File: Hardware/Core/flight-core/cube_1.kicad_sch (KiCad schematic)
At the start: 3 parts, among them J5 Cube Orange Plus Female Header

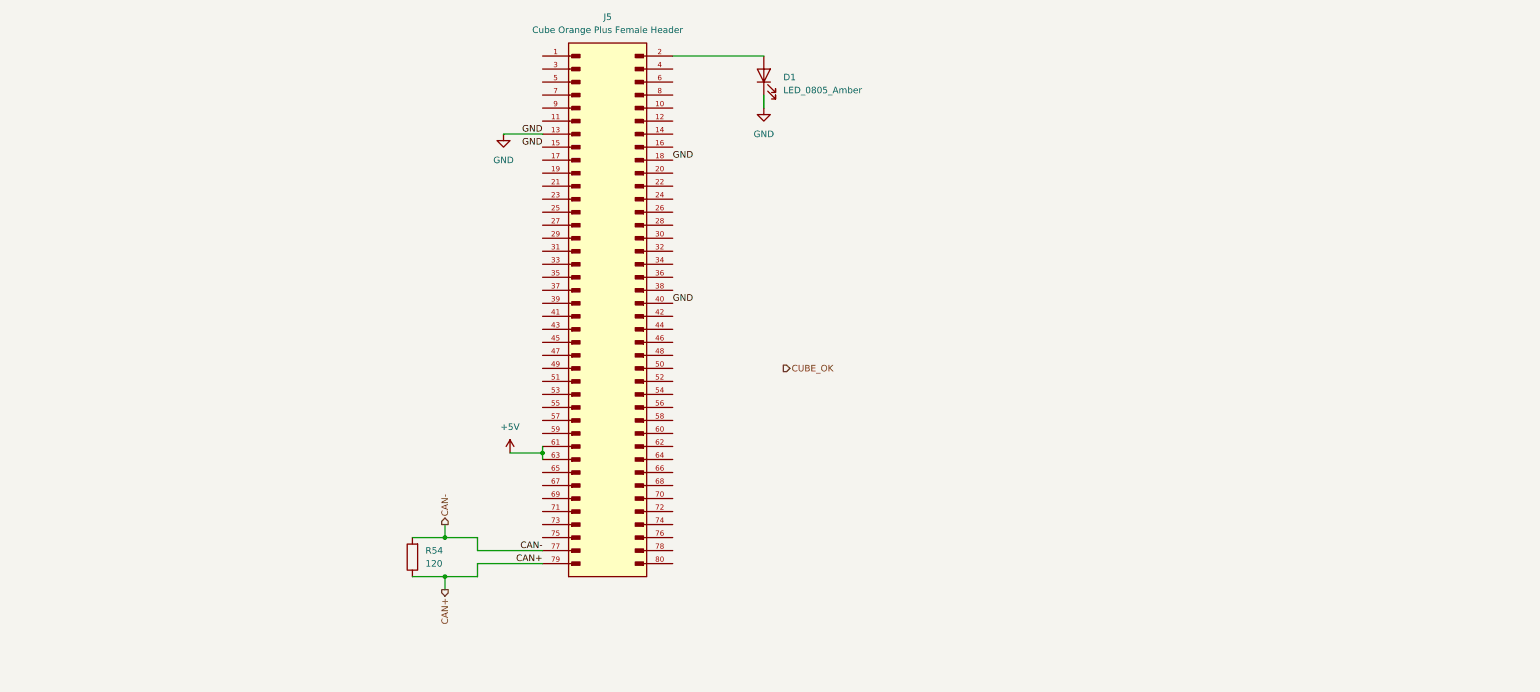
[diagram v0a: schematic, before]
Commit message: added all cube pins and corrected cube shdn node
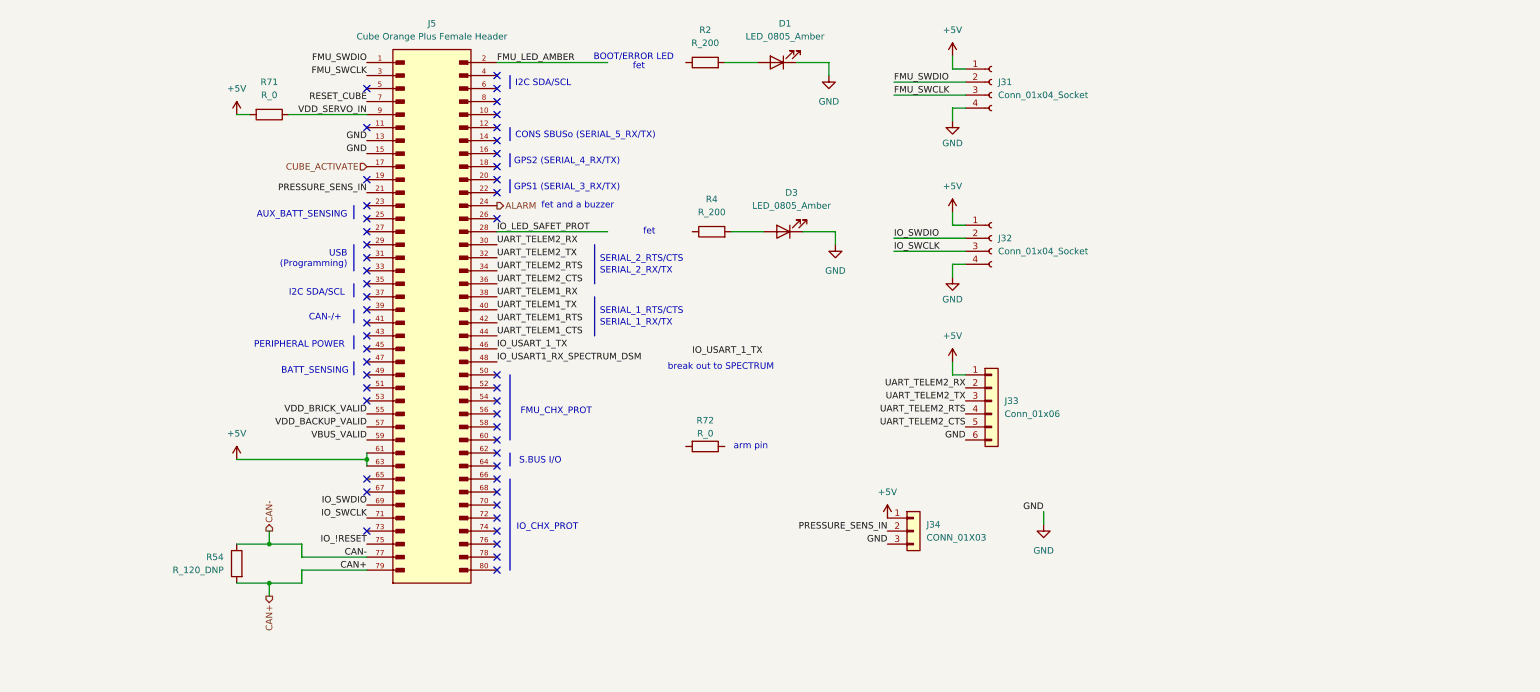
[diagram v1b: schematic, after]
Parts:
- removed R54: 120, OEM:R_0603, symbol OEM:120R
- added D3: LED_0805_Amber, footprints:LED_0805_OEM, symbol formula:LED_0805_Amber
- added J31, J32: Conn_01x04_Socket, Connector_PinSocket_2.54mm:PinSocket_1x04_P2.54mm_Vertical, symbol Connector:Conn_01x04_Socket
- added J33: Conn_01x06, symbol Connector_Generic:Conn_01x06
- added J34: CONN_01X03, Pin_Headers:Pin_Header_Straight_1x03_Pitch2.54mm, symbol formula:CONN_01X03
- added R2, R4: R_200, footprints:R_0603_1608Metric, symbol formula:R_200
- added R54: R_120_DNP, footprints:R_0603_1608Metric, symbol formula:R_120_DNP
- added R71, R72: R_0, footprints:R_0603_1608Metric, symbol formula:R_0
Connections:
- net +5V: now also J31.1 (Pin_1), J32.1 (Pin_1), J33.1 (Pin_1), J34.1 (P1), R71.2
- net CAN+: now also R54.2
- net CAN-: now also R54.1
- net GND: now also D3.1 (K), J31.4 (Pin_4), J32.4 (Pin_4), J33.6 (Pin_6), J34.3 (P3); no longer J5.18, J5.40
- net FMU_SWDIO: now reaches J5.1
- net FMU_SWDIO: now also J31.2 (Pin_2)
- net CUBE_ACTIVATE: now reaches J5.17
- net at D1.2 (A): now also R2.2; no longer J5.2
- net PRESSURE_SENS_IN: now reaches J5.21
- net PRESSURE_SENS_IN: now also J34.2 (P2)
- net ALARM: now reaches J5.24
- net IO_LED_SAFET_PROT: now reaches J5.28
- net FMU_SWCLK: now reaches J5.3
- net FMU_SWCLK: now also J31.3 (Pin_3)
- net UART_TELEM2_RX: now reaches J5.30
- net UART_TELEM2_RX: now also J33.2 (Pin_2)
- net UART_TELEM2_TX: now reaches J5.32
- net UART_TELEM2_TX: now also J33.3 (Pin_3)
- net UART_TELEM2_RTS: now reaches J5.34
- net UART_TELEM2_RTS: now also J33.4 (Pin_4)
- net UART_TELEM2_CTS: now reaches J5.36
- net UART_TELEM2_CTS: now also J33.5 (Pin_5)
- net UART_TELEM1_RX: now reaches J5.38
- net UART_TELEM1_RTS: now reaches J5.42
- net UART_TELEM1_CTS: now reaches J5.44
- net IO_USART_1_TX: now reaches J5.46
- net IO_USART1_RX_SPECTRUM_DSM: now reaches J5.48
- net VDD_BRICK_VALID: now reaches J5.55
- net VDD_BACKUP_VALID: now reaches J5.57
- net VBUS_VALID: now reaches J5.59
- net IO_SWDIO: now reaches J5.69
- net IO_SWDIO: now also J32.2 (Pin_2)
- net RESET_CUBE: now reaches J5.7
- net IO_SWCLK: now reaches J5.71
- net IO_SWCLK: now also J32.3 (Pin_3)
- net IO_!RESET: now reaches J5.75
- net VDD_SERVO_IN: now reaches J5.9
- net VDD_SERVO_IN: now also R71.1
- new net: D3.2 (A), R4.2
- new net FMU_LED_AMBER: J5.2
- new net UART_TELEM1_TX: J5.40
- no-connect marks 0 -> 49
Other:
- note added: "AUX_BATT_SENSING"
- note added: "BATT_SENSING"
- note added: "BOOT/ERROR LED"
- note added: "CAN-/+"
- note added: "CONS SBUSo (SERIAL_5_RX/TX)"
- note added: "FMU_CHX_PROT"
- note added: "GPS1 (SERIAL_3_RX/TX)"
- note added: "GPS2 (SERIAL_4_RX/TX)"
- note added: "I2C SDA/SCL"
- note added: "IO_CHX_PROT"
- note added: "PERIPHERAL POWER"
- note added: "S.BUS I/O"
- note added: "SERIAL_1_RTS/CTS"
- note added: "SERIAL_1_RX/TX"
- note added: "SERIAL_2_RTS/CTS"
- note added: "SERIAL_2_RX/TX"
- note added: "USB (Programming)"
- note added: "arm pin"
- note added: "break out to SPECTRUM"
- note added: "fet"
- note added: "fet and a buzzer"
- moved on the sheet: J5

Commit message: added telemetry header
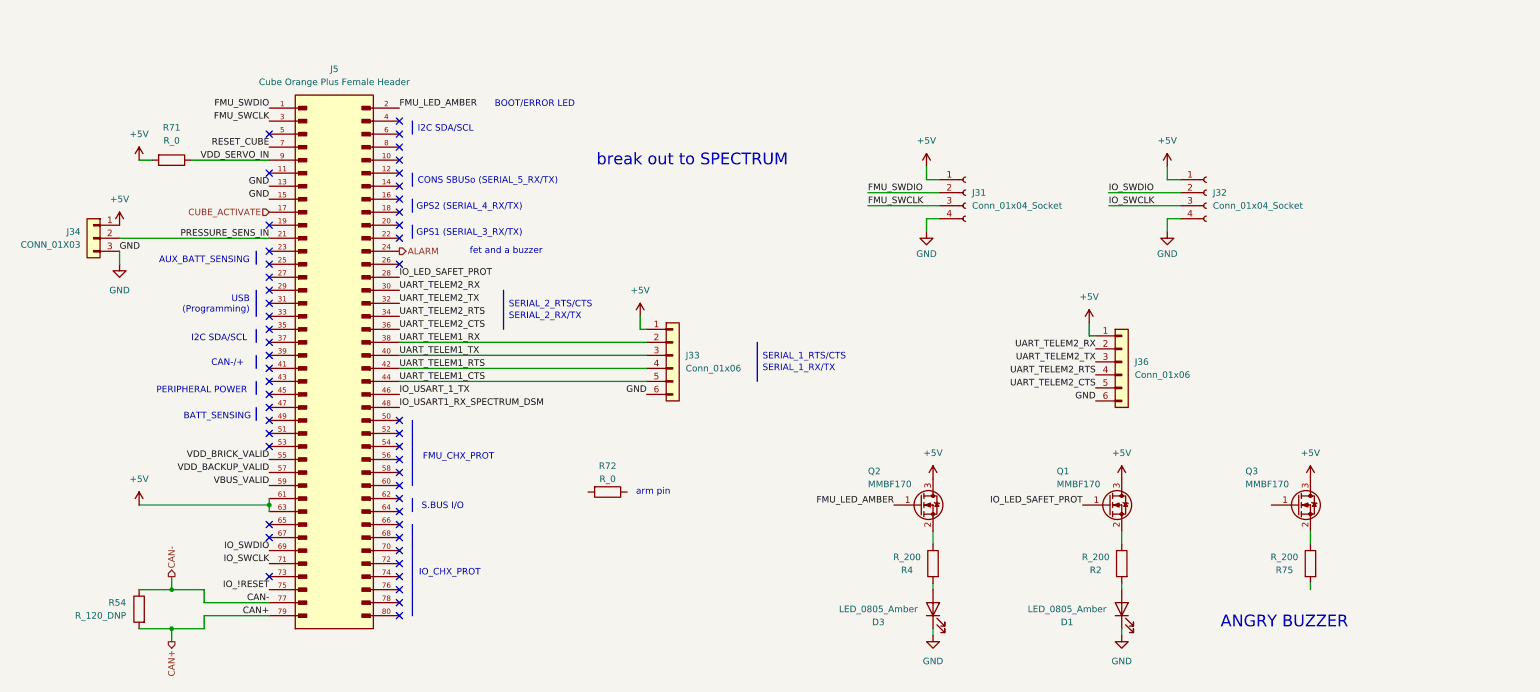
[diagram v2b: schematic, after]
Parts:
- added J36: Conn_01x06, symbol Connector_Generic:Conn_01x06
- added Q1, Q2, Q3: MMBF170, TO_SOT_Packages_SMD:SOT-23, symbol formula:MMBF170
- added R75: R_200, footprints:R_0603_1608Metric, symbol formula:R_200
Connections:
- net +5V: now also J36.1 (Pin_1), Q1.3 (D), Q2.3 (D), Q3.3 (D)
- net FMU_LED_AMBER: now also Q2.1 (G)
- net GND: now also J36.6 (Pin_6)
- net IO_LED_SAFET_PROT: now also Q1.1 (G)
- net UART_TELEM1_CTS: now also J33.5 (Pin_5)
- net UART_TELEM1_RTS: now also J33.4 (Pin_4)
- net UART_TELEM1_RX: now also J33.2 (Pin_2)
- net UART_TELEM1_TX: now also J33.3 (Pin_3)
- net UART_TELEM2_CTS: now also J36.5 (Pin_5); no longer J33.5 (Pin_5)
- net UART_TELEM2_RTS: now also J36.4 (Pin_4); no longer J33.4 (Pin_4)
- net UART_TELEM2_RX: now also J36.2 (Pin_2); no longer J33.2 (Pin_2)
- net UART_TELEM2_TX: now also J36.3 (Pin_3); no longer J33.3 (Pin_3)
- net at R2.1: now also Q1.2 (S)
- net at R4.1: now also Q2.2 (S)
- new net: Q3.2 (S), R75.1
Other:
- note added: "ANGRY BUZZER"
- note removed: "fet"
- moved on the sheet: J31, J32, J33, J34, J5, R54, R71, R72

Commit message: top sheet reorg
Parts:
- removed R72: R_0, footprints:R_0603_1608Metric, symbol formula:R_0
- renumbered D3 to D21, D1 to D22, J34 to J38, J5 to J39, J33 to J40, J31 to J41, J36 to J42, J32 to J43, Q2 to Q17, Q1 to Q18, Q3 to Q19, R2 to R100, R75 to R107, R54 to R72, R71 to R98, R4 to R99
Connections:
- net ALARM: now also Q19.1 (G)
- net IO_!RESET renamed IO_~{RESET}
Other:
- note removed: "arm pin"
- moved on the sheet: J41, J43

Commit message: updated all top sheets
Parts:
- removed R107: R_200, footprints:R_0603_1608Metric, symbol formula:R_200
- added J2: CONN_01X03, Pin_Headers:Pin_Header_Straight_1x03_Pitch2.54mm, symbol formula:CONN_01X03
- added TP13: TP, footprints:tp_1.6mm, symbol formula:TP
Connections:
- net GND: now also J2.3 (P3)
- net IO_USART1_RX_SPECTRUM_DSM: now also J2.2 (P2), TP13.1 (TP)
- net SHDN_CRITICAL: now reaches J39.50
- net FINAL_SHDN: now reaches J39.52
- new net +3.3V: J2.1 (P1)
- no-connect marks 49 -> 47
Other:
- note added: "BUZZER"
- note removed: "ANGRY BUZZER"
- note removed: "break out to SPECTRUM"
- moved on the sheet: J41, J42, J43

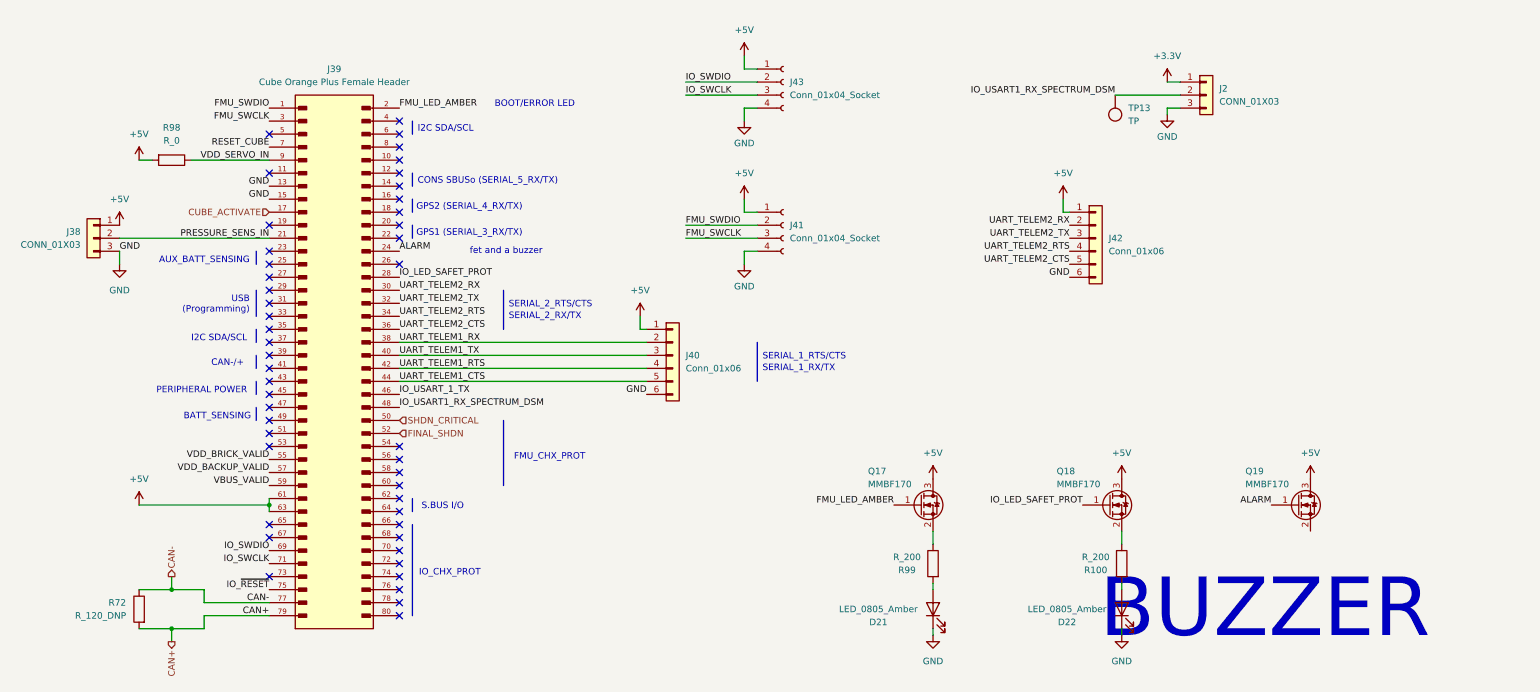
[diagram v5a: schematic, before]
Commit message: ERC fixes + reset cube signal
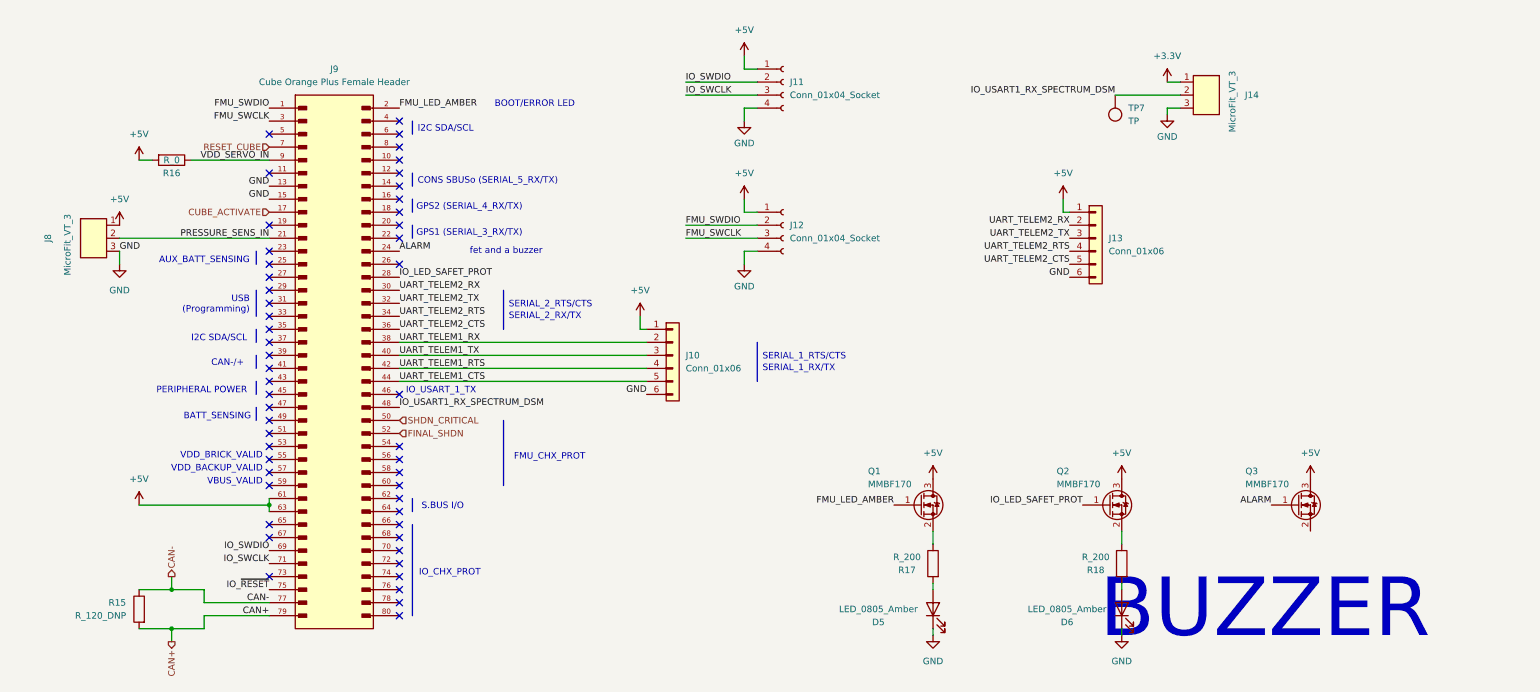
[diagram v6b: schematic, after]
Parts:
- removed J2, J38: CONN_01X03, Pin_Headers:Pin_Header_Straight_1x03_Pitch2.54mm, symbol formula:CONN_01X03
- removed J39: Cube Orange Plus Female Header, DF17_4.0_-80DP-0.5V_57_:HRS_DF17_4.0_-80DP-0.5V_57_, symbol formula:DF17_4.0_-80DP-0.5V_57_
- added J14, J8: MicroFit_VT_3, footprints:MicroFit_VT_3, symbol formula:MicroFit_VT_3
- added J9: Cube Orange Plus Female Header, obad_footprints:Cube_Orange+_Female_Header, symbol OlinBAD:DF17_4.0_-80DP-0.5V_57_
- J10: renamed from J40; footprint (none) -> footprints:MicroFit_VT_6
- J13: renamed from J42; footprint (none) -> footprints:MicroFit_VT_6
- Q1: renamed from Q17; footprint TO_SOT_Packages_SMD:SOT-23 -> Package_TO_SOT_SMD:SOT-23
- Q2: renamed from Q18; footprint TO_SOT_Packages_SMD:SOT-23 -> Package_TO_SOT_SMD:SOT-23
- Q3: renamed from Q19; footprint TO_SOT_Packages_SMD:SOT-23 -> Package_TO_SOT_SMD:SOT-23
- renumbered D21 to D5, D22 to D6, J43 to J11, J41 to J12, R72 to R15, R98 to R16, R99 to R17, R100 to R18, TP13 to TP7
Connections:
- net +3.3V: now also J14.1
- net +5V: now also J8.1, J9.61, J9.63
- net ALARM: now also J9.24
- net CAN+: now also J9.79
- net CAN-: now also J9.77
- net CUBE_ACTIVATE: now also J9.17
- net FINAL_SHDN: now also J9.52
- net FMU_LED_AMBER: now also J9.2
- net FMU_SWCLK: now also J9.3
- net FMU_SWDIO: now also J9.1
- net GND: now also J14.3, J8.3, J9.13, J9.15
- net IO_LED_SAFET_PROT: now also J9.28
- net IO_SWCLK: now also J9.71
- net IO_SWDIO: now also J9.69
- net IO_USART1_RX_SPECTRUM_DSM: now also J14.2, J9.48
- net IO_~{RESET}: now also J9.75
- net PRESSURE_SENS_IN: now also J8.2, J9.21
- net RESET_CUBE: now also J9.7
- net SHDN_CRITICAL: now also J9.50
- net UART_TELEM1_CTS: now also J9.44
- net UART_TELEM1_RTS: now also J9.42
- net UART_TELEM1_RX: now also J9.38
- net UART_TELEM1_TX: now also J9.40
- net UART_TELEM2_CTS: now also J9.36
- net UART_TELEM2_RTS: now also J9.34
- net UART_TELEM2_RX: now also J9.30
- net UART_TELEM2_TX: now also J9.32
- net VDD_SERVO_IN: now also J9.9
- no-connect marks 47 -> 51
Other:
- note added: "IO_USART_1_TX"
- note added: "VBUS_VALID"
- note added: "VDD_BACKUP_VALID"
- note added: "VDD_BRICK_VALID"
